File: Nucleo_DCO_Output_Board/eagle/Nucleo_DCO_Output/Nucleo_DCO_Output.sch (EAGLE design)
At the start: 38 parts, among them CN1 9VPWR, IC1 TLE2426LP, IC2 NJM4580, IC3 NJM4580

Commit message: Nucleo_DCO_PSU
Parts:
- R15: value 12k -> 120k
- R16: value 3.3k -> 33k
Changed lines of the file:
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@@
 <part name="JP4" library="pinhead" library_urn="urn:adsk.eagle:library:325" deviceset="PINHD-1X2" device="" package3d_urn="urn:adsk.eagle:package:22435/2" value="TP_GND"/>
 <part name="GND13" library="supply1" library_urn="urn:adsk.eagle:library:371" deviceset="GND" device=""/>
-<part name="R15" library="rcl" library_urn="urn:adsk.eagle:library:334" deviceset="R-EU_" device="0207/7" package3d_urn="urn:adsk.eagle:package:23493/1" value="12k"/>
-<part name="R16" library="rcl" library_urn="urn:adsk.eagle:library:334" deviceset="R-EU_" device="0207/7" package3d_urn="urn:adsk.eagle:package:23493/1" value="3.3k"/>
+<part name="R15" library="rcl" library_urn="urn:adsk.eagle:library:334" deviceset="R-EU_" device="0207/7" package3d_urn="urn:adsk.eagle:package:23493/1" value="120k"/>
+<part name="R16" library="rcl" library_urn="urn:adsk.eagle:library:334" deviceset="R-EU_" device="0207/7" package3d_urn="urn:adsk.eagle:package:23493/1" value="33k"/>
 <part name="GND14" library="supply1" library_urn="urn:adsk.eagle:library:371" deviceset="GND" device=""/>
 <part name="JP5" library="pinhead" library_urn="urn:adsk.eagle:library:325" deviceset="PINHD-1X2" device="" package3d_urn="urn:adsk.eagle:package:22435/2" value="PW_WATCH"/>

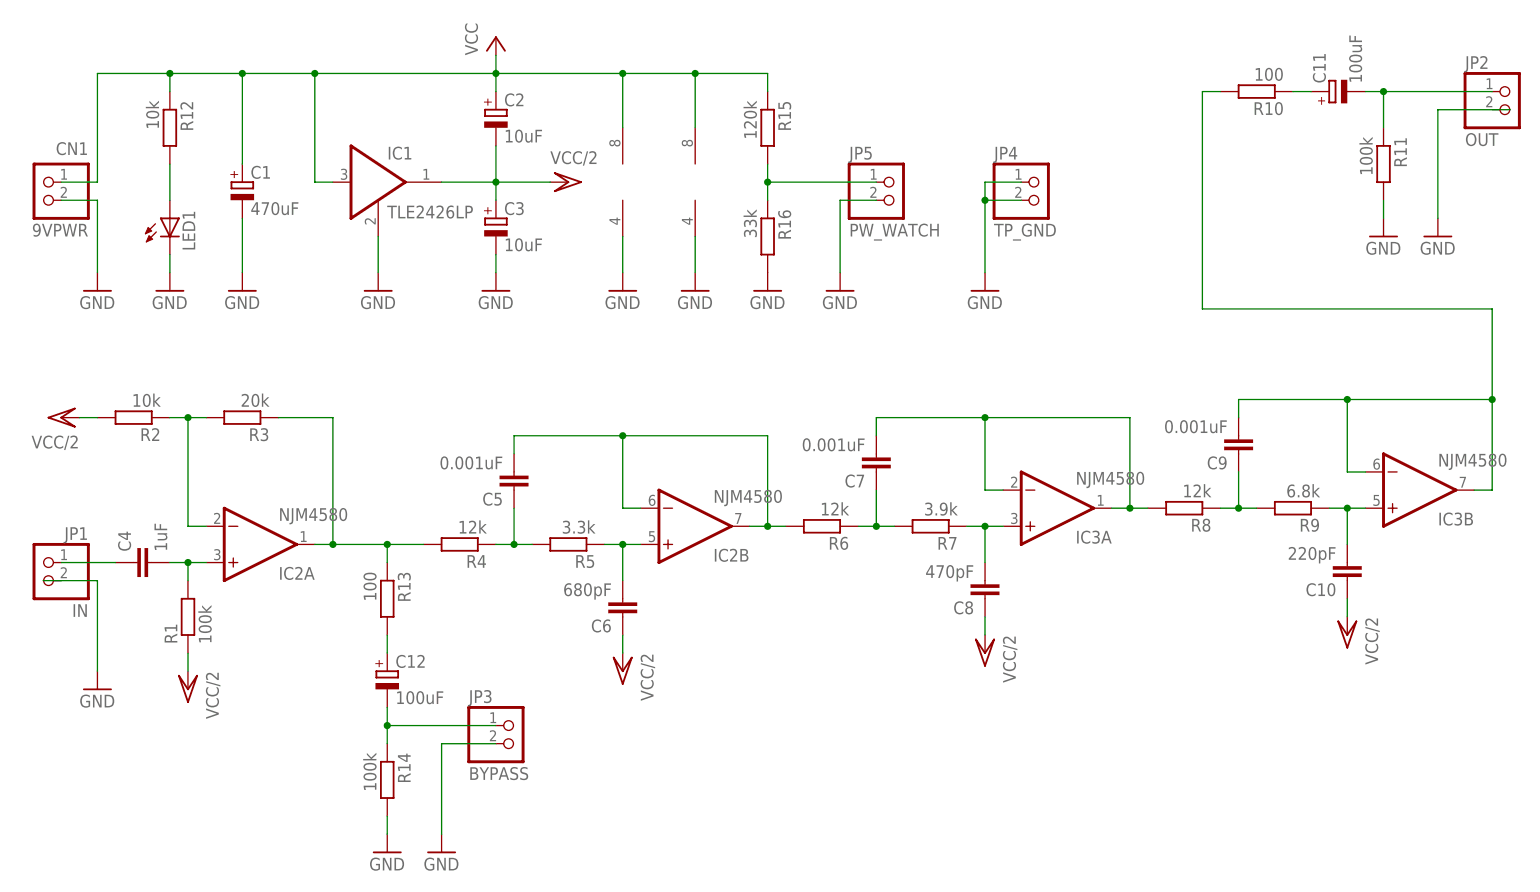
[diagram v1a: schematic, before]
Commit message: Update: Nucleo_DCO_Output (add de-coupling cap)
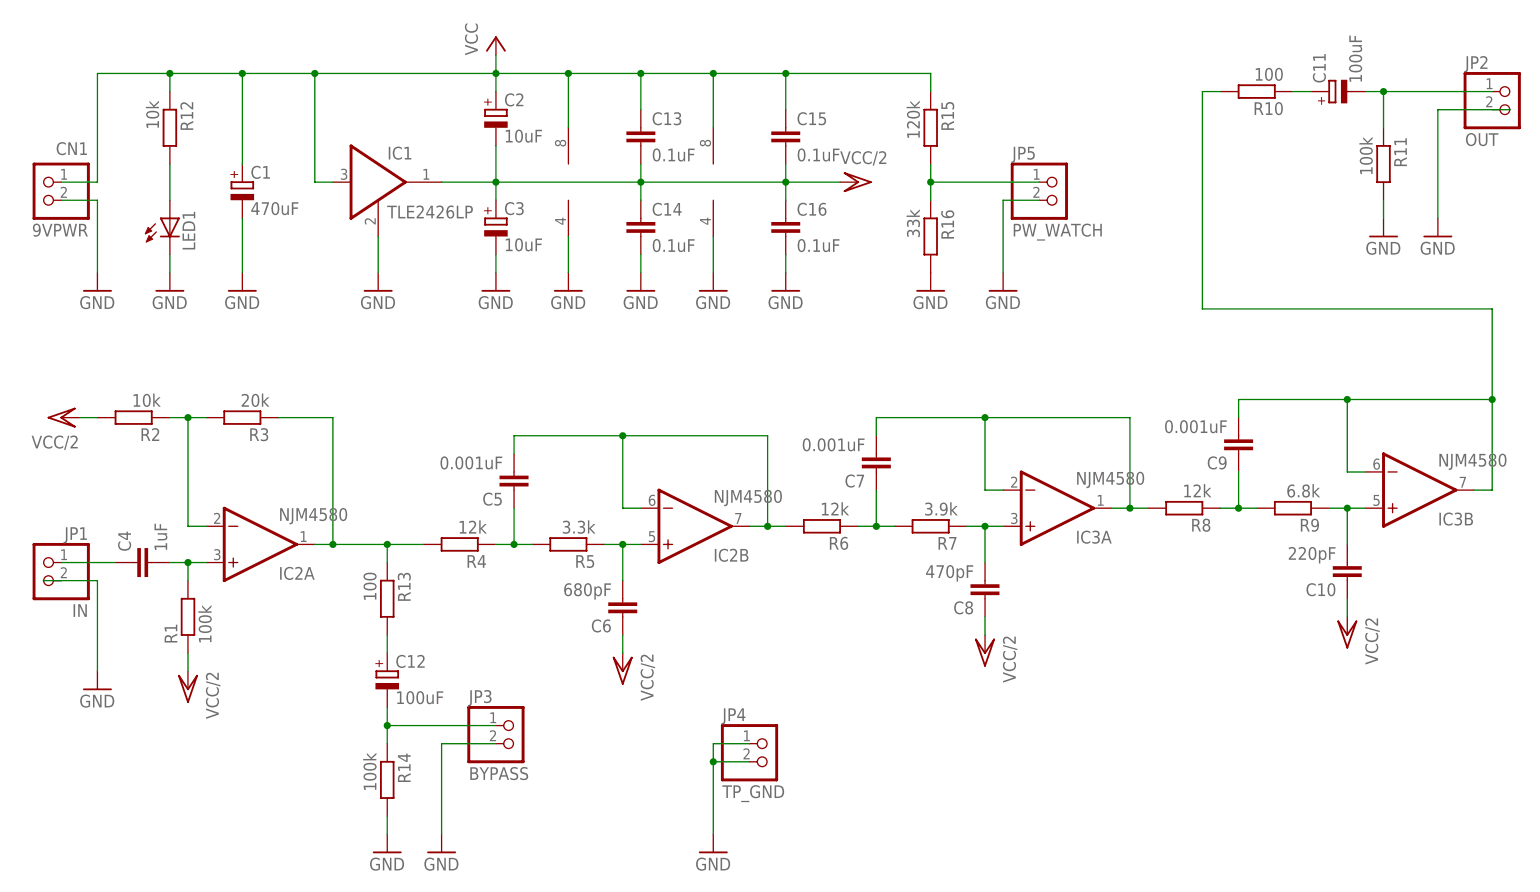
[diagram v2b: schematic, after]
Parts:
- added C13, C15, C16: 0.1uF, rcl:C-EU025-024X044
- added C14: 0.1uF, rcl:C-EU050-024X044
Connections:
- net GND: now also C14.2, C16.2
- net VCC: now also C13.1, C15.1
- net VCC/2: now also C13.2, C14.1, C15.2, C16.1
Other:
- moved on the sheet: JP4, JP5, R15, R16
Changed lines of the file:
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@@
 <part name="JP5" library="pinhead" library_urn="urn:adsk.eagle:library:325" deviceset="PINHD-1X2" device="" package3d_urn="urn:adsk.eagle:package:22435/2" value="PW_WATCH"/>
 <part name="GND15" library="supply1" library_urn="urn:adsk.eagle:library:371" deviceset="GND" device=""/>
+<part name="C13" library="rcl" library_urn="urn:adsk.eagle:library:334" deviceset="C-EU" device="025-024X044" package3d_urn="urn:adsk.eagle:package:23630/1" value="0.1uF"/>
+<part name="C14" library="rcl" library_urn="urn:adsk.eagle:library:334" deviceset="C-EU" device="050-024X044" package3d_urn="urn:adsk.eagle:package:23643/1" value="0.1uF"/>
+<part name="C15" library="rcl" library_urn="urn:adsk.eagle:library:334" deviceset="C-EU" device="025-024X044" package3d_urn="urn:adsk.eagle:package:23630/1" value="0.1uF"/>
+<part name="C16" library="rcl" library_urn="urn:adsk.eagle:library:334" deviceset="C-EU" device="025-024X044" package3d_urn="urn:adsk.eagle:package:23630/1" value="0.1uF"/>
+<part name="GND16" library="supply1" library_urn="urn:adsk.eagle:library:371" deviceset="GND" device=""/>
+<part name="GND17" library="supply1" library_urn="urn:adsk.eagle:library:371" deviceset="GND" device=""/>
 </parts>
 <sheets>
@@
 <instance part="C3" gate="G$1" x="91.44" y="119.38"/>
 <instance part="GND4" gate="1" x="91.44" y="109.22"/>
-<instance part="P+1" gate="G$1" x="101.6" y="124.46" rot="R270"/>
+<instance part="P+1" gate="G$1" x="142.24" y="124.46" rot="R270"/>
 <instance part="P+2" gate="VCC" x="91.44" y="144.78"/>
 <instance part="JP1" gate="G$1" x="27.94" y="68.58" rot="MR0"/>
@@
 <instance part="GND8" gate="1" x="83.82" y="30.48"/>
 <instance part="FRAME1" gate="G$1" x="0" y="0"/>
-<instance part="IC2" gate="P" x="109.22" y="124.46"/>
-<instance part="GND11" gate="1" x="109.22" y="109.22"/>
-<instance part="IC3" gate="P" x="119.38" y="124.46"/>
-<instance part="GND12" gate="1" x="119.38" y="109.22"/>
-<instance part="JP4" gate="G$1" x="167.64" y="121.92"/>
-<instance part="GND13" gate="1" x="160.02" y="109.22"/>
-<instance part="R15" gate="G$1" x="129.54" y="132.08" rot="R270"/>
-<instance part="R16" gate="G$1" x="129.54" y="116.84" rot="R270"/>
-<instance part="GND14" gate="1" x="129.54" y="109.22"/>
-<instance part="JP5" gate="G$1" x="147.32" y="121.92"/>
-<instance part="GND15" gate="1" x="139.7" y="109.22"/>
+<instance part="IC2" gate="P" x="101.6" y="124.46"/>
+<instance part="GND11" gate="1" x="101.6" y="109.22"/>
+<instance part="IC3" gate="P" x="121.92" y="124.46"/>
+<instance part="GND12" gate="1" x="121.92" y="109.22"/>
+<instance part="JP4" gate="G$1" x="129.54" y="43.18"/>
+<instance part="GND13" gate="1" x="121.92" y="30.48"/>
+<instance part="R15" gate="G$1" x="152.4" y="132.08" rot="R270"/>
+<instance part="R16" gate="G$1" x="152.4" y="116.84" rot="R270"/>
+<instance part="GND14" gate="1" x="152.4" y="109.22"/>
+<instance part="JP5" gate="G$1" x="170.18" y="121.92"/>
+<instance part="GND15" gate="1" x="162.56" y="109.22"/>
+<instance part="C13" gate="G$1" x="111.76" y="132.08"/>
+<instance part="C14" gate="G$1" x="111.76" y="119.38"/>
+<instance part="C15" gate="G$1" x="132.08" y="132.08"/>
+<instance part="C16" gate="G$1" x="132.08" y="119.38"/>
+<instance part="GND16" gate="1" x="111.76" y="109.22"/>
+<instance part="GND17" gate="1" x="132.08" y="109.22"/>
 </instances>
 <busses>
@@
 <pinref part="GND11" gate="1" pin="GND"/>
 <pinref part="IC2" gate="P" pin="V-"/>
-<wire x1="109.22" y1="111.76" x2="109.22" y2="116.84" width="0.1524" layer="91"/>
+<wire x1="101.6" y1="111.76" x2="101.6" y2="116.84" width="0.1524" layer="91"/>
 </segment>
 <segment>
 <pinref part="GND12" gate="1" pin="GND"/>
 <pinref part="IC3" gate="P" pin="V-"/>
-<wire x1="119.38" y1="111.76" x2="119.38" y2="116.84" width="0.1524" layer="91"/>
+<wire x1="121.92" y1="111.76" x2="121.92" y2="116.84" width="0.1524" layer="91"/>
 </segment>
 <segment>
 <pinref part="JP4" gate="G$1" pin="1"/>
-<wire x1="165.1" y1="124.46" x2="160.02" y2="124.46" width="0.1524" layer="91"/>
+<wire x1="127" y1="45.72" x2="121.92" y2="45.72" width="0.1524" layer="91"/>
 <pinref part="GND13" gate="1" pin="GND"/>
-<wire x1="160.02" y1="124.46" x2="160.02" y2="121.92" width="0.1524" layer="91"/>
+<wire x1="121.92" y1="45.72" x2="121.92" y2="43.18" width="0.1524" layer="91"/>
 <pinref part="JP4" gate="G$1" pin="2"/>
-<wire x1="160.02" y1="121.92" x2="160.02" y2="111.76" width="0.1524" layer="91"/>
-<wire x1="165.1" y1="121.92" x2="160.02" y2="121.92" width="0.1524" layer="91"/>
-<junction x="160.02" y="121.92"/>
+<wire x1="121.92" y1="43.18" x2="121.92" y2="33.02" width="0.1524" layer="91"/>
+<wire x1="127" y1="43.18" x2="121.92" y2="43.18" width="0.1524" layer="91"/>
+<junction x="121.92" y="43.18"/>
 </segment>
 <segment>
@@
 <segment>
 <pinref part="JP5" gate="G$1" pin="2"/>
-<wire x1="144.78" y1="121.92" x2="139.7" y2="121.92" width="0.1524" layer="91"/>
+<wire x1="167.64" y1="121.92" x2="162.56" y2="121.92" width="0.1524" layer="91"/>
 <pinref part="GND15" gate="1" pin="GND"/>
-<wire x1="139.7" y1="121.92" x2="139.7" y2="111.76" width="0.1524" layer="91"/>
+<wire x1="162.56" y1="121.92" x2="162.56" y2="111.76" width="0.1524" layer="91"/>
+</segment>
+<segment>
+<pinref part="C14" gate="G$1" pin="2"/>
+<pinref part="GND16" gate="1" pin="GND"/>
+<wire x1="111.76" y1="114.3" x2="111.76" y2="111.76" width="0.1524" layer="91"/>
+</segment>
+<segment>
+<pinref part="C16" gate="G$1" pin="2"/>
+<pinref part="GND17" gate="1" pin="GND"/>
+<wire x1="132.08" y1="114.3" x2="132.08" y2="111.76" width="0.1524" layer="91"/>
 </segment>
 </net>
@@
 <junction x="91.44" y="124.46"/>
 <pinref part="P+1" gate="G$1" pin="VCC/2"/>
-<wire x1="99.06" y1="124.46" x2="91.44" y2="124.46" width="0.1524" layer="91"/>
+<wire x1="139.7" y1="124.46" x2="132.08" y2="124.46" width="0.1524" layer="91"/>
+<pinref part="C14" gate="G$1" pin="1"/>
+<wire x1="132.08" y1="124.46" x2="111.76" y2="124.46" width="0.1524" layer="91"/>
+<wire x1="111.76" y1="124.46" x2="91.44" y2="124.46" width="0.1524" layer="91"/>
+<wire x1="111.76" y1="121.92" x2="111.76" y2="124.46" width="0.1524" layer="91"/>
+<junction x="111.76" y="124.46"/>
+<pinref part="C13" gate="G$1" pin="2"/>
+<wire x1="111.76" y1="127" x2="111.76" y2="124.46" width="0.1524" layer="91"/>
+<pinref part="C15" gate="G$1" pin="2"/>
+<wire x1="132.08" y1="127" x2="132.08" y2="124.46" width="0.1524" layer="91"/>
+<junction x="132.08" y="124.46"/>
+<pinref part="C16" gate="G$1" pin="1"/>
+<wire x1="132.08" y1="121.92" x2="132.08" y2="124.46" width="0.1524" layer="91"/>
 </segment>
 <segment>
@@
 <pinref part="IC2" gate="P" pin="V+"/>
 <wire x1="66.04" y1="139.7" x2="91.44" y2="139.7" width="0.1524" layer="91"/>
-<wire x1="91.44" y1="139.7" x2="109.22" y2="139.7" width="0.1524" layer="91"/>
-<wire x1="109.22" y1="139.7" x2="109.22" y2="132.08" width="0.1524" layer="91"/>
+<wire x1="91.44" y1="139.7" x2="101.6" y2="139.7" width="0.1524" layer="91"/>
+<wire x1="101.6" y1="139.7" x2="101.6" y2="132.08" width="0.1524" layer="91"/>
 <pinref part="IC3" gate="P" pin="V+"/>
-<wire x1="119.38" y1="132.08" x2="119.38" y2="139.7" width="0.1524" layer="91"/>
-<wire x1="119.38" y1="139.7" x2="109.22" y2="139.7" width="0.1524" layer="91"/>
-<junction x="109.22" y="139.7"/>
+<wire x1="121.92" y1="132.08" x2="121.92" y2="139.7" width="0.1524" layer="91"/>
+<wire x1="121.92" y1="139.7" x2="111.76" y2="139.7" width="0.1524" layer="91"/>
+<junction x="101.6" y="139.7"/>
 <pinref part="IC1" gate="G$1" pin="I"/>
+<wire x1="111.76" y1="139.7" x2="101.6" y2="139.7" width="0.1524" layer="91"/>
 <wire x1="68.58" y1="124.46" x2="66.04" y2="124.46" width="0.1524" layer="91"/>
 <wire x1="66.04" y1="124.46" x2="66.04" y2="139.7" width="0.1524" layer="91"/>
 <junction x="66.04" y="139.7"/>
 <pinref part="R15" gate="G$1" pin="1"/>
-<wire x1="129.54" y1="137.16" x2="129.54" y2="139.7" width="0.1524" layer="91"/>
-<wire x1="129.54" y1="139.7" x2="119.38" y2="139.7" width="0.1524" layer="91"/>
-<junction x="119.38" y="139.7"/>
+<wire x1="152.4" y1="137.16" x2="152.4" y2="139.7" width="0.1524" layer="91"/>
+<wire x1="152.4" y1="139.7" x2="132.08" y2="139.7" width="0.1524" layer="91"/>
+<junction x="121.92" y="139.7"/>
+<pinref part="C13" gate="G$1" pin="1"/>
+<wire x1="132.08" y1="139.7" x2="121.92" y2="139.7" width="0.1524" layer="91"/>
+<wire x1="111.76" y1="134.62" x2="111.76" y2="139.7" width="0.1524" layer="91"/>
+<junction x="111.76" y="139.7"/>
+<pinref part="C15" gate="G$1" pin="1"/>
+<wire x1="132.08" y1="134.62" x2="132.08" y2="139.7" width="0.1524" layer="91"/>
+<junction x="132.08" y="139.7"/>
 </segment>
 </net>
@@
 <pinref part="R16" gate="G$1" pin="1"/>
 <pinref part="R15" gate="G$1" pin="2"/>
-<wire x1="129.54" y1="121.92" x2="129.54" y2="124.46" width="0.1524" layer="91"/>
+<wire x1="152.4" y1="121.92" x2="152.4" y2="124.46" width="0.1524" layer="91"/>
 <pinref part="JP5" gate="G$1" pin="1"/>
-<wire x1="129.54" y1="124.46" x2="129.54" y2="127" width="0.1524" layer="91"/>
-<wire x1="144.78" y1="124.46" x2="129.54" y2="124.46" width="0.1524" layer="91"/>
-<junction x="129.54" y="124.46"/>
-</segment>
-</net>
+<wire x1="152.4" y1="124.46" x2="152.4" y2="127" width="0.1524" layer="91"/>
+<wire x1="167.64" y1="124.46" x2="152.4" y2="124.46" width="0.1524" layer="91"/>
+<junction x="152.4" y="124.46"/>
+</segment>
+</net>
